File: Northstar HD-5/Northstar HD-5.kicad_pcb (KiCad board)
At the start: 2 copper layers, 190.6 x 165 mm, 123 parts, among them J1 MFM data, J2 MFM control, P1 northstar card edge, Q1 2N3904, U1A1 26LS32, U1B1 26LS31, U1C1 74S10, U1D1 74S00, U1E1 50ns_Delay, U1F1 74S04, U1H1 74LS123, U1K1 LM393, U1L1 7438, U1M1 74LS374, U2A1 100ns_Delay, U2B1 74LS161, U2C1 74LS74, U2D1 74LS175, U2E1 82S129, U2F1 74S174, U2H1 74LS283, U2J1 74LS393, U2K1 74LS393, U2L1 2114, U2M1 2114, U3A1 74S74, U3B1 74S02, U3C1 74LS161, U3D1 74LS04, U3E1 74LS161, U3F1 74LS393, U3H1 74LS273, U3J1 74LS193, U3K1 74LS164, U3L1 74LS374, U3M1 74LS166, U4A1 74S74, U4B1 74S02, U4C1 74S74, U4D1 74S04, U4F1 74LS193, U4H1 74LS193, U4J1 74LS04, U4K1 74LS244, U4L1 74LS244, U4M1 74LS244, U5D1 74S124, U5F1 74S74, U5H1 74LS32, U5J1 74LS00, U5K1 74LS279, U5L1 74LS138, U5M1 74LS138

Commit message: placed components for column 5
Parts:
- added ?: , , F.Cu at (178.6, 15.0)
- added ?: , , F.Cu at (178.6, 29.9)
- added C22: 47nF, Capacitor_THT:C_Disc_D10.0mm_W2.5mm_P5.00mm, F.Cu at (154.8, 103.2)
- added C23: 47nF, Capacitor_THT:C_Disc_D10.0mm_W2.5mm_P5.00mm, F.Cu at (154.8, 131.1)
- added C24: 47nF, Capacitor_THT:C_Disc_D10.0mm_W2.5mm_P5.00mm, F.Cu at (154.8, 145.0)
- added C25: 47nF, Capacitor_THT:C_Disc_D10.0mm_W2.5mm_P5.00mm, F.Cu at (52.6, -261.1)
- added C26: 47nF, Capacitor_THT:C_Disc_D10.0mm_W2.5mm_P5.00mm, F.Cu at (52.8, -249.9)
- added C27: 47nF, Capacitor_THT:C_Disc_D10.0mm_W2.5mm_P5.00mm, F.Cu at (53.1, -237.5)
- added C28: 47nF, Capacitor_THT:C_Disc_D10.0mm_W2.5mm_P5.00mm, F.Cu at (53.8, -91.4)
- added C29: 47nF, Capacitor_THT:C_Disc_D10.0mm_W2.5mm_P5.00mm, F.Cu at (56.1, -140.0)
- added C30: 47nF, Capacitor_THT:C_Disc_D10.0mm_W2.5mm_P5.00mm, F.Cu at (53.3, -125.2)
- added C31: 47nF, Capacitor_THT:C_Disc_D10.0mm_W2.5mm_P5.00mm, F.Cu at (53.1, -109.9)
- CR1, CR2, CR3: footprint Diode_THT:D_A-405_P12.70mm_Horizontal -> Evan's misc parts:D_A-405_P12.70mm_Horizontal_NORTH
- R1, R12, R14, R18, R19, R2, R20, R21, R22, R23, R26, R27, R28, R3, R4, R5, R6, R7: footprint Resistor_THT:R_Axial_DIN0309_L9.0mm_D3.2mm_P12.70mm_Horizontal -> Evan's misc parts:R_Axial_DIN0309_L9.0mm_D3.2mm_P12.70mm_Horizontal_NORTH
- R10, R11, R15, R16, R17, R24, R25, R29, R8, R9: footprint Resistor_THT:R_Axial_DIN0207_L6.3mm_D2.5mm_P15.24mm_Horizontal -> Evan's misc parts:R_Axial_DIN0207_L6.3mm_D2.5mm_P15.24mm_Horizontal_NORTH
- moved U5K1 397.6 mm to (160.1, 124.6), turned to 90 degrees
- moved C19 374.3 mm to (174.1, 42.2), turned to -90 degrees
- moved C3 373.9 mm to (-336.7, -137.6)
- moved R5 373.9 mm to (-337.2, -143.2)
- moved U1E1 373.9 mm to (-348.0, -143.5)
- moved TP6 371.0 mm to (53.1, -240.8)
- moved TP13 366.1 mm to (69.6, -252.0)
- moved C17 365.4 mm to (53.1, -224.8), turned to -90 degrees
- moved R13 362.2 mm to (168.4, 34.5), turned to 180 degrees
- moved R15 362.0 mm to (147.4, 36.4)
- moved R20 360.7 mm to (75.9, -183.4), turned to 180 degrees
- moved R4 351.4 mm to (154.8, 114.0), turned to -90 degrees
- moved R10 350.3 mm to (77.5, -201.4), turned to 180 degrees
- moved TP5 348.3 mm to (182.2, 12.8)
- moved U4F1 346.1 mm to (59.9, -161.8), turned to 90 degrees
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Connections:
- C19 pad 1: Net-(R13-Pad1) -> Net-(C19-Pad1)
- R13 pad 1: Net-(R13-Pad1) -> GND
- R13 pad 3: GND -> Net-(C19-Pad1)
- R14 pad 1: Net-(R13-Pad1) -> Net-(C19-Pad1)
- R15 pad 2: Net-(R13-Pad1) -> Net-(C19-Pad1)
- R2 pad 2: /Power and pullups/PU2 -> PU2
- R29 pad 1: Net-(R13-Pad1) -> Net-(C19-Pad1)
- R4 pad 2: /Power and pullups/PU4 -> PU4
- U2B1 pad 10: /HD5 Sheet 2/PU2 -> PU2
- U2B1 pad 7: /HD5 Sheet 2/PU2 -> PU2
- U2B1 pad 9: /HD5 Sheet 2/PU2 -> PU2
- U3A1 pad 13: /HD5 Sheet 2/PU2 -> PU2
- U3A1 pad 4: /HD5 Sheet 2/PU2 -> PU2
- U4A1 pad 1: /HD5 Sheet 2/PU2 -> PU2
- U4A1 pad 10: /HD5 Sheet 2/PU2 -> PU2
- U4A1 pad 13: /HD5 Sheet 2/PU2 -> PU2
- U4C1 pad 1: /HD5 Sheet 2/PU2 -> PU2
- U4C1 pad 10: /HD5 Sheet 2/PU2 -> PU2
- U5D1 pad 3: Net-(R13-Pad1) -> Net-(C19-Pad1)
- U5L1 pad 6: /HD5 Sheet 1/PU4 -> PU4
- U5M1 pad 6: /HD5 Sheet 1/PU4 -> PU4
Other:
- board text added: "+V5"
- board text added: "1"
- board text added: "2"
- board text added: "30"
- board text added: "LS00"
- board text added: "LS138"
- board text added: "LS279"
- board text added: "LS32"
- board text added: "S124"
- board text added: "S74"

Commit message: placed components and repaired multi sheet labels
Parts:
- removed ? (x2): , 
- removed the C18 at (-408.1, -52.6)
- removed the C20 at (-346.5, 102.0)
- added C32: 47nF, Evan's misc parts:C_Disc_D10.0mm_W2.5mm_P5.00mm_NORTH, F.Cu at (85.2, 5.12)
- added C33: 47nF, Evan's misc parts:C_Disc_D10.0mm_W2.5mm_P5.00mm_NORTH, F.Cu at (88.9, 19.1)
- added C34: 47nF, Evan's misc parts:C_Disc_D10.0mm_W2.5mm_P5.00mm_NORTH, F.Cu at (88.9, 47.1)
- added C35: 47nF, Evan's misc parts:C_Disc_D10.0mm_W2.5mm_P5.00mm_NORTH, F.Cu at (88.9, 75.2)
- added C36: 47nF, Evan's misc parts:C_Disc_D10.0mm_W2.5mm_P5.00mm_NORTH, F.Cu at (88.9, 103.1)
- added C37: 47nF, Evan's misc parts:C_Disc_D10.0mm_W2.5mm_P5.00mm_NORTH, F.Cu at (85.2, 131.1)
- added C38: 47nF, Evan's misc parts:C_Disc_D10.0mm_W2.5mm_P5.00mm_NORTH, F.Cu at (54.8, 5.12)
- added C39: 47nF, Evan's misc parts:C_Disc_D10.0mm_W2.5mm_P5.00mm_NORTH, F.Cu at (54.8, 19.1)
- added C40: 47nF, Evan's misc parts:C_Disc_D10.0mm_W2.5mm_P5.00mm_NORTH, F.Cu at (54.8, 47.1)
- added C41: 47nF, Evan's misc parts:C_Disc_D10.0mm_W2.5mm_P5.00mm_NORTH, F.Cu at (54.9, 66.3)
- added C42: 47nF, Evan's misc parts:C_Disc_D10.0mm_W2.5mm_P5.00mm_NORTH, F.Cu at (54.8, 75.2)
- added C43: 47nF, Evan's misc parts:C_Disc_D10.0mm_W2.5mm_P5.00mm_NORTH, F.Cu at (57.1, 103.1)
- added C44: 47nF, Evan's misc parts:C_Disc_D10.0mm_W2.5mm_P5.00mm_NORTH, F.Cu at (54.5, 131.1)
- added C45: 47nF, Evan's misc parts:C_Disc_D10.0mm_W2.5mm_P5.00mm_NORTH, F.Cu at (54.5, 145.0)
- added C46: 47nF, Evan's misc parts:C_Disc_D10.0mm_W2.5mm_P5.00mm_NORTH, F.Cu at (23.0, 5.12)
- added C47: 47nF, Evan's misc parts:C_Disc_D10.0mm_W2.5mm_P5.00mm_NORTH, F.Cu at (23.0, 19.1)
- added C48: 47nF, Evan's misc parts:C_Disc_D10.0mm_W2.5mm_P5.00mm_NORTH, F.Cu at (25.5, 33.2)
- added C49: 47nF, Evan's misc parts:C_Disc_D10.0mm_W2.5mm_P5.00mm_NORTH, F.Cu at (25.5, 47.1)
- added C50: 47nF, Evan's misc parts:C_Disc_D10.0mm_W2.5mm_P5.00mm_NORTH, F.Cu at (23.0, 61.3)
- added C51: 47nF, Evan's misc parts:C_Disc_D10.0mm_W2.5mm_P5.00mm_NORTH, F.Cu at (25.5, 75.2)
- added C52: 47nF, Evan's misc parts:C_Disc_D10.0mm_W2.5mm_P5.00mm_NORTH, F.Cu at (23.0, 101.8)
- added C53: 47nF, Evan's misc parts:C_Disc_D10.0mm_W2.5mm_P5.00mm_NORTH, F.Cu at (25.5, 131.1)
- added C54: 47nF, Evan's misc parts:C_Disc_D10.0mm_W2.5mm_P5.00mm_NORTH, F.Cu at (20.4, 145.0)
- C12, C13, C14, C15, C19, C22, C23, C24, C25, C26, C27, C28, C29, C30, C31: footprint Capacitor_THT:C_Disc_D10.0mm_W2.5mm_P5.00mm -> Evan's misc parts:C_Disc_D10.0mm_W2.5mm_P5.00mm_NORTH
- C17: renamed from C16; footprint Capacitor_THT:C_Disc_D10.0mm_W2.5mm_P5.00mm -> Evan's misc parts:C_Disc_D10.0mm_W2.5mm_P5.00mm_NORTH
- C18: renamed from C17; footprint Capacitor_THT:C_Disc_D10.0mm_W2.5mm_P5.00mm -> Evan's misc parts:C_Disc_D10.0mm_W2.5mm_P5.00mm_NORTH
- C20: renamed from C21; footprint Capacitor_THT:C_Disc_D10.0mm_W2.5mm_P5.00mm -> Evan's misc parts:C_Disc_D10.0mm_W2.5mm_P5.00mm_NORTH
- U1K1: footprint Package_DIP:DIP-8-16_W7.62mm -> Package_DIP:DIP-8_W7.62mm
- moved U3L1 576.8 mm to (91.5, 138.6), turned to 90 degrees
- moved U3M1 557.1 mm to (94.1, 152.5), turned to 90 degrees
- moved U2M1 552.6 mm to (59.7, 152.5), turned to 90 degrees
- moved U2L1 538.3 mm to (59.7, 138.6), turned to 90 degrees
- moved U1M1 535.6 mm to (25.5, 152.5), turned to 90 degrees
- moved U3K1 522.5 mm to (94.1, 124.6), turned to 90 degrees
- moved U2F1 499.2 mm to (59.7, 82.7), turned to 90 degrees
- moved U2E1 482.3 mm to (59.7, 68.7), turned to 90 degrees
- moved R25 475.7 mm to (17.9, 97.1), turned to 180 degrees
- moved U3H1 475.0 mm to (91.5, 96.7), turned to 90 degrees
- moved U2D1 466.6 mm to (59.7, 54.7), turned to 90 degrees
- moved C12 466.2 mm to (40.9, 117.0), turned to -90 degrees
- moved R24 463.1 mm to (2.63, 100.2)
- moved U3J1 457.8 mm to (94.1, 110.7), turned to 90 degrees
- moved R26 457.7 mm to (15.3, 94.0), turned to 180 degrees
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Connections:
- net /HD5 Sheet 1/RA0 renamed RA0
- net /HD5 Sheet 1/RA1 renamed RA1
- net /HD5 Sheet 1/RA2 renamed RA2
- net /HD5 Sheet 1/RA3 renamed RA3
- net /HD5 Sheet 1/RA5 renamed RA5
- net /HD5 Sheet 1/RA6 renamed RA6
- net /HD5 Sheet 1/RA7 renamed RA7
- net /HD5 Sheet 1/RA8 renamed RA8
- net /HD5 Sheet 1/RA9 renamed RA9
- net /HD5 Sheet 1/SD01 renamed SD01
- net /HD5 Sheet 1/SD02 renamed SD02
- net /HD5 Sheet 1/SD03 renamed SD03
- net /HD5 Sheet 1/SD04 renamed SD04
- net /HD5 Sheet 1/SD05 renamed SD05
- net /HD5 Sheet 1/SD06 renamed SD06
- net /HD5 Sheet 1/SD07 renamed SD07
- net /HD5 Sheet 1/WR DATA renamed WR DATA
- net /HD5 Sheet 1//CLR ADD renamed /CLR ADD
- net /HD5 Sheet 1//RD STAT renamed /RD STAT
- net /HD5 Sheet 2/2.5Mhz renamed 2.5Mhz
- net /HD5 Sheet 2/EN SYNC renamed EN SYNC
- net /HD5 Sheet 2/INT SEC P renamed INT SEC P
- net /HD5 Sheet 2/Phase Lock renamed Phase Lock
- net /HD5 Sheet 2/READ DATA renamed READ DATA
- net /HD5 Sheet 2/VCO Out renamed VCO Out
- net /HD5 Sheet 2//INT SEC P renamed /INT SEC P
- net /HD5 Sheet 2//RD CLK renamed /RD CLK
- net /Power and pullups/IO 8MHz renamed IO 8MHz
- net /Power and pullups/IO A3 renamed IO A3
- net /Power and pullups//BIO RES renamed /BIO RES
- net /Power and pullups//IO INT renamed /IO INT
- C20 pad 1: +5V -> +5VP
- J1 pad 1: /Power and pullups//SE_EC -> /SE_EC
- J1 pad 13: /Power and pullups/MFM W+ -> MFM W+
- J1 pad 14: /Power and pullups/MFM W- -> MFM W-
- J1 pad 17: /Power and pullups/MFM RD+ -> MFM RD+
- J1 pad 18: /Power and pullups/MFM RD- -> MFM RD-
- J2 pad 10: /Power and pullups//TRK0_PHI -> /TRK0_PHI
- J2 pad 12: /Power and pullups//WR FLT -> /WR FLT
- J2 pad 14: /Power and pullups/HS0 -> HS0
- J2 pad 18: /Power and pullups/HS1 -> HS1
- J2 pad 2: /Power and pullups//LOW CUR -> /LOW CUR
- J2 pad 20: /Power and pullups//INDEX -> /INDEX
- J2 pad 22: /Power and pullups//RDY -> /RDY
- J2 pad 24: /Power and pullups//STEP -> /STEP
- J2 pad 34: /Power and pullups//DIR / PRCMP -> /DIR / PRCMP
- J2 pad 4: /Power and pullups//HS2 -> /HS2
- J2 pad 6: /Power and pullups//WR GATE -> /WR GATE
- J2 pad 8: /Power and pullups//SK COMP -> /SK COMP
- P1 pad 11: /Power and pullups/IO A1 -> IO A1
- P1 pad 13: /Power and pullups//BRD -> /BRD
- P1 pad 14: /Power and pullups/IO A0 -> IO A0
- P1 pad 16: /Power and pullups//BWR -> /BWR
- P1 pad 17: /Power and pullups/IO3 -> IO3
- P1 pad 19: /Power and pullups/IO2 -> IO2
- P1 pad 20: /Power and pullups/IO4 -> IO4
- P1 pad 22: /Power and pullups/IO5 -> IO5
- P1 pad 23: /Power and pullups/IO6 -> IO6
- P1 pad 24: /Power and pullups/IO1 -> IO1
- P1 pad 25: /Power and pullups/IO0 -> IO0
- P1 pad 28: /Power and pullups/IO7 -> IO7
- P1 pad 29: /Power and pullups//SELECT -> /SELECT
- P1 pad 3: /Power and pullups//ID REQ -> IO6
- P1 pad 9: /Power and pullups/IO A2 -> IO A2
- Q1 pad 3: /HD5 Sheet 1//WR GATE -> /WR GATE
- R1 pad 2: /Power and pullups/PU1 -> PU1
- R26 pad 2: /HD5 Sheet 1/1WR GATE -> 1WR GATE
- R27 pad 2: /HD5 Sheet 1/1WR GATE -> 1WR GATE
- R3 pad 2: /Power and pullups/PU3 -> PU3
- R7 pad 1: /HD5 Sheet 2/MFM RD- -> MFM RD-
- R7 pad 2: /HD5 Sheet 2/MFM RD+ -> MFM RD+
- RN1 pad 2: /Power and pullups//INDEX -> /INDEX
- RN1 pad 3: /Power and pullups//RDY -> /RDY
- RN1 pad 4: /Power and pullups//SE_EC -> /SE_EC
- RN1 pad 5: /Power and pullups//SK0COMP -> /SK COMP
- RN1 pad 6: /Power and pullups//TRK0_PHI -> /TRK0_PHI
- RN1 pad 7: /Power and pullups//WR FLT -> /WR FLT
- RN2 pad 2: /Power and pullups/ID0 -> ID0
- RN2 pad 3: /Power and pullups/ID4 -> ID4
- RN2 pad 4: /Power and pullups/ID5 -> ID5
- RN2 pad 5: /Power and pullups/ID1 -> ID1
- RN2 pad 6: /Power and pullups/ID2 -> ID2
- RN2 pad 7: /Power and pullups/ID6 -> ID6
- RN2 pad 8: /Power and pullups/ID7 -> ID7
- RN2 pad 9: /Power and pullups/ID3 -> ID3
- TP1 pad 1: /HD5 Sheet 2/5MHz -> 5MHz
- TP12 pad 1: /HD5 Sheet 2//RD BYT RDY -> /RD BYT RDY
- TP3 pad 1: /HD5 Sheet 2/RD CLK -> RD CLK
- U1A1 pad 1: /HD5 Sheet 2/MFM RD- -> MFM RD-
- U1A1 pad 2: /HD5 Sheet 2/MFM RD+ -> MFM RD+
- U1B1 pad 5: /HD5 Sheet 1/MFM W- -> MFM W-
- U1B1 pad 6: /HD5 Sheet 1/MFM W+ -> MFM W+
- U1C1 pad 10: /HD5 Sheet 2//RD RAM -> /RD RAM
- U1C1 pad 9: /HD5 Sheet 2//HOST WR RAM -> /HOST WR RAM
- U1D1 pad 6: /HD5 Sheet 2//LD WR BYTE -> /LD WR BYTE
- U1F1 pad 9: /HD5 Sheet 2//HOST WR RAM -> /HOST WR RAM
- U1H1 pad 1: /HD5 Sheet 2//INDEX -> /INDEX
- U1H1 pad 2: /HD5 Sheet 2/PU3 -> PU3
- U1H1 pad 3: /HD5 Sheet 2//FORMAT WR -> /FORMAT WR
- U1H1 pad 9: /HD5 Sheet 2/CNTR INDEX -> CNTR INDEX
- U1L1 pad 3: /HD5 Sheet 1//STEP -> /STEP
- U1L1 pad 8: /HD5 Sheet 1//HS2 -> /HS2
- U1M1 pad 11: /HD5 Sheet 1//LD CONT -> /LD CONT
- U1M1 pad 12: /HD5 Sheet 1//LOW CUR -> /LOW CUR
- U1M1 pad 13: /HD5 Sheet 1/ID3 -> ID3
- U1M1 pad 14: /HD5 Sheet 1/ID2 -> ID2
- U1M1 pad 16: /HD5 Sheet 1/HS1 -> HS1
- U1M1 pad 17: /HD5 Sheet 1/ID1 -> ID1
- U1M1 pad 18: /HD5 Sheet 1/ID0 -> ID0
- U1M1 pad 19: /HD5 Sheet 1/HS0 -> HS0
- U1M1 pad 3: /HD5 Sheet 1/ID4 -> ID4
- U1M1 pad 4: /HD5 Sheet 1/ID5 -> ID5
- U1M1 pad 5: /HD5 Sheet 1//DIR / PRCMP -> /DIR / PRCMP
- U1M1 pad 7: /HD5 Sheet 1/ID6 -> ID6
- U1M1 pad 8: /HD5 Sheet 1/ID7 -> ID7
- U1M1 pad 9: /HD5 Sheet 1/HEADER READ -> HEADER READ
- U2B1 pad 12: /HD5 Sheet 2/RAW INDEX -> RAW INDEX
- U2C1 pad 1: /HD5 Sheet 2/RD GATE -> RD GATE
- U2C1 pad 10: /HD5 Sheet 2/PU1 -> PU1
- U2C1 pad 11: /HD5 Sheet 2/5MHz -> 5MHz
- U2C1 pad 13: /HD5 Sheet 2/PU1 -> PU1
- U2C1 pad 2: /HD5 Sheet 2/RD GATE -> RD GATE
- U2C1 pad 3: /HD5 Sheet 2/SD00 -> SD00
- U2C1 pad 4: /HD5 Sheet 2/PU1 -> PU1
- U2D1 pad 1: /HD5 Sheet 1/PU 3 -> PU3
- U2D1 pad 2: /HD5 Sheet 1/5MHz -> 5MHz
- U2E1 pad 1: /HD5 Sheet 1//DIR / PRCMP -> /DIR / PRCMP
- U2E1 pad 2: /HD5 Sheet 1/1WR GATE -> 1WR GATE
- U2E1 pad 3: /HD5 Sheet 1/5MHz -> 5MHz
- U2F1 pad 1: /HD5 Sheet 1/PU 3 -> PU3
- U2F1 pad 15: /HD5 Sheet 1/SYNC INDEX -> SYNC INDEX
- U2F1 pad 3: /HD5 Sheet 1/RAW INDEX -> RAW INDEX
- U2F1 pad 9: /HD5 Sheet 1/5MHz -> 5MHz
- U2H1 pad 11: /HD5 Sheet 2/PU3 -> PU3
- U2H1 pad 2: /HD5 Sheet 2/PU3 -> PU3
- U2H1 pad 6: /HD5 Sheet 2/PU3 -> PU3
- U2J1 pad 12: /HD5 Sheet 2/SYNC INDEX -> SYNC INDEX
- U2K1 pad 3: /HD5 Sheet 1/RA4 -> RA4
- U2L1 pad 10: /HD5 Sheet 1//WR RAM -> /WR RAM
- U2L1 pad 11: /HD5 Sheet 1/ID 3 -> ID3
- U2L1 pad 12: /HD5 Sheet 1/ID 2 -> ID2
- U2L1 pad 13: /HD5 Sheet 1/ID 1 -> ID1
- U2L1 pad 14: /HD5 Sheet 1/ID 0 -> ID0
- U2L1 pad 17: /HD5 Sheet 1/RA4 -> RA4
- U2L1 pad 8: /HD5 Sheet 1//SEL RAM -> /SEL RAM
- U2M1 pad 10: /HD5 Sheet 1//WR RAM -> /WR RAM
- U2M1 pad 11: /HD5 Sheet 1/ID 7 -> ID7
- U2M1 pad 12: /HD5 Sheet 1/ID 6 -> ID6
- U2M1 pad 13: /HD5 Sheet 1/ID 5 -> ID5
- U2M1 pad 14: /HD5 Sheet 1/ID 4 -> ID4
- U2M1 pad 17: /HD5 Sheet 1/RA4 -> RA4
- U2M1 pad 8: /HD5 Sheet 1//SEL RAM -> /SEL RAM
- U3A1 pad 5: /HD5 Sheet 2/SEP RD DATA -> SEP RD DATA
- U3B1 pad 1: /HD5 Sheet 2//WR RAM -> /WR RAM
- U3B1 pad 13: /HD5 Sheet 2//SEL RAM -> /SEL RAM
- U3B1 pad 4: /HD5 Sheet 2/RD CLK -> RD CLK
- U3B1 pad 9: /HD5 Sheet 2/RD CLK -> RD CLK
- U3C1 pad 10: /HD5 Sheet 2/PU1 -> PU1
- U3C1 pad 3: /HD5 Sheet 2/PU1 -> PU1
- U3C1 pad 7: /HD5 Sheet 2/PU1 -> PU1
- U3C1 pad 9: /HD5 Sheet 2//RD BYT RDY -> /RD BYT RDY
- U3D1 pad 10: /HD5 Sheet 2//RD DATA TO RAM -> /RD DATA TO RAM
- U3D1 pad 8: /HD5 Sheet 2//RD BYT RDY -> /RD BYT RDY
- U3E1 pad 1: /HD5 Sheet 2/1WR GATE -> 1WR GATE
- U3E1 pad 10: /HD5 Sheet 2/PU1 -> PU1
- U3E1 pad 2: /HD5 Sheet 2/5MHz -> 5MHz
- U3E1 pad 3: /HD5 Sheet 2/PU1 -> PU1
- U3E1 pad 4: /HD5 Sheet 2/PU1 -> PU1
- U3E1 pad 7: /HD5 Sheet 2/PU1 -> PU1
- U3E1 pad 9: /HD5 Sheet 2//LD WR BYTE -> /LD WR BYTE
- U3F1 pad 12: /HD5 Sheet 2/SYNC INDEX -> SYNC INDEX
- U3F1 pad 2: /HD5 Sheet 2/SYNC INDEX -> SYNC INDEX
- U3H1 pad 1: /HD5 Sheet 2/PU3 -> PU3
- U3H1 pad 11: /HD5 Sheet 2/SYNC INDEX -> SYNC INDEX
- U3J1 pad 5: /HD5 Sheet 2/PU3 -> PU3
- U3K1 pad 1: /HD5 Sheet 1/SEP RD DATA -> SEP RD DATA
- U3K1 pad 2: /HD5 Sheet 1/SEP RD DATA -> SEP RD DATA
- U3K1 pad 3: /HD5 Sheet 1/SD00 -> SD00
- U3K1 pad 8: /HD5 Sheet 1/RD CLK -> RD CLK
- U3K1 pad 9: /HD5 Sheet 1/RD GATE -> RD GATE
- U3L1 pad 1: /HD5 Sheet 1//RD DATA TO RAM -> /RD DATA TO RAM
- U3L1 pad 11: /HD5 Sheet 1//RD BYT RDY -> /RD BYT RDY
- U3L1 pad 12: /HD5 Sheet 1/ID3 -> ID3
- U3L1 pad 15: /HD5 Sheet 1/ID2 -> ID2
- U3L1 pad 16: /HD5 Sheet 1/ID1 -> ID1
- U3L1 pad 18: /HD5 Sheet 1/SD00 -> SD00
- U3L1 pad 19: /HD5 Sheet 1/ID0 -> ID0
- U3L1 pad 2: /HD5 Sheet 1/ID7 -> ID7
- U3L1 pad 5: /HD5 Sheet 1/ID6 -> ID6
- U3L1 pad 6: /HD5 Sheet 1/ID5 -> ID5
- U3L1 pad 9: /HD5 Sheet 1/ID4 -> ID4
- U3M1 pad 10: /HD5 Sheet 1/ID4 -> ID4
- U3M1 pad 11: /HD5 Sheet 1/ID5 -> ID5
- U3M1 pad 12: /HD5 Sheet 1/ID6 -> ID6
- U3M1 pad 14: /HD5 Sheet 1/ID7 -> ID7
- U3M1 pad 15: /HD5 Sheet 1//LD WR BYTE -> /LD WR BYTE
- U3M1 pad 2: /HD5 Sheet 1/ID0 -> ID0
- U3M1 pad 3: /HD5 Sheet 1/ID1 -> ID1
- U3M1 pad 4: /HD5 Sheet 1/ID2 -> ID2
- U3M1 pad 5: /HD5 Sheet 1/ID3 -> ID3
- U3M1 pad 7: /HD5 Sheet 1/5MHz -> 5MHz
- U3M1 pad 9: /HD5 Sheet 1/1WR GATE -> 1WR GATE
- U4F1 pad 5: /HD5 Sheet 2/PU4 -> PU4
- U4F1 pad 9: /HD5 Sheet 2/PU4 -> PU4
- U4H1 pad 5: /HD5 Sheet 2/PU4 -> PU4
- U4J1 pad 11: /HD5 Sheet 1//SEL RAM -> /SEL RAM
- U4J1 pad 2: /HD5 Sheet 2//H TO ID -> /H TO ID
- U4J1 pad 5: /HD5 Sheet 2/SYNC INDEX -> SYNC INDEX
- U4K1 pad 11: /HD5 Sheet 1//RDY -> /RDY
- U4K1 pad 12: /HD5 Sheet 1/HD3 -> IO3
- U4K1 pad 13: /HD5 Sheet 1/CNTR INDEX -> CNTR INDEX
- U4K1 pad 14: /HD5 Sheet 1/HD2 -> IO2
- U4K1 pad 15: /HD5 Sheet 1/R/W ACTIVE -> R/W ACTIVE
- U4K1 pad 16: /HD5 Sheet 1/HD1 -> IO1
- U4K1 pad 17: /HD5 Sheet 1/CNTR SECTOR -> CNTR SECTOR
- U4K1 pad 18: /HD5 Sheet 1/HD0 -> IO0
- U4K1 pad 2: /HD5 Sheet 1//WR FLT -> /WR FLT
- U4K1 pad 3: /HD5 Sheet 1/HD7 -> IO7
- U4K1 pad 4: /HD5 Sheet 1//SK COMP -> /SK COMP
- U4K1 pad 5: /HD5 Sheet 1/HD6 -> IO6
- U4K1 pad 6: /HD5 Sheet 1//TRK0_PHI -> /TRK0_PHI
- U4K1 pad 7: /HD5 Sheet 1/HD5 -> IO5
- U4K1 pad 8: /HD5 Sheet 1//SE_EC -> /SE_EC
- U4K1 pad 9: /HD5 Sheet 1/HD4 -> IO4
- U4L1 pad 1: /HD5 Sheet 1//H TO ID -> /H TO ID
- U4L1 pad 11: /HD5 Sheet 1/HD3 -> IO3
- U4L1 pad 12: /HD5 Sheet 1/ID4 -> ID4
- U4L1 pad 13: /HD5 Sheet 1/HD2 -> IO2
- U4L1 pad 14: /HD5 Sheet 1/ID5 -> ID5
- U4L1 pad 15: /HD5 Sheet 1/HD1 -> IO1
- U4L1 pad 16: /HD5 Sheet 1/ID6 -> ID6
- U4L1 pad 17: /HD5 Sheet 1/HD0 -> IO0
- U4L1 pad 18: /HD5 Sheet 1/ID7 -> ID7
- U4L1 pad 19: /HD5 Sheet 1//H TO ID -> /H TO ID
- U4L1 pad 2: /HD5 Sheet 1/HD7 -> IO7
- U4L1 pad 3: /HD5 Sheet 1/ID0 -> ID0
- U4L1 pad 4: /HD5 Sheet 1/HD6 -> IO6
- U4L1 pad 5: /HD5 Sheet 1/ID1 -> ID1
- U4L1 pad 6: /HD5 Sheet 1/HD5 -> IO5
- U4L1 pad 7: /HD5 Sheet 1/ID2 -> ID2
- U4L1 pad 8: /HD5 Sheet 1/HD4 -> IO4
- U4L1 pad 9: /HD5 Sheet 1/ID3 -> ID3
- U4M1 pad 1: /HD5 Sheet 1//RD RAM -> /RD RAM
- U4M1 pad 11: /HD5 Sheet 1/ID 3 -> ID3
- U4M1 pad 12: /HD5 Sheet 1/HD3 -> IO3
- U4M1 pad 13: /HD5 Sheet 1/ID 2 -> ID2
- U4M1 pad 14: /HD5 Sheet 1/HD2 -> IO2
- U4M1 pad 15: /HD5 Sheet 1/ID 1 -> ID1
- U4M1 pad 16: /HD5 Sheet 1/HD1 -> IO1
- U4M1 pad 17: /HD5 Sheet 1/ID 0 -> ID0
- U4M1 pad 18: /HD5 Sheet 1/HD0 -> IO0
- U4M1 pad 19: /HD5 Sheet 1//RD RAM -> /RD RAM
- U4M1 pad 2: /HD5 Sheet 1/ID 7 -> ID7
- U4M1 pad 3: /HD5 Sheet 1/HD7 -> IO7
- U4M1 pad 4: /HD5 Sheet 1/ID 6 -> ID6
- U4M1 pad 5: /HD5 Sheet 1/HD6 -> IO6
- U4M1 pad 6: /HD5 Sheet 1/ID 5 -> ID5
- U4M1 pad 7: /HD5 Sheet 1/HD5 -> IO5
- U4M1 pad 8: /HD5 Sheet 1/ID 4 -> ID4
- U4M1 pad 9: /HD5 Sheet 1/HD4 -> IO4
- U5F1 pad 1: /HD5 Sheet 2/PU4 -> PU4
- U5F1 pad 10: /HD5 Sheet 2//START READ -> /START READ
- U5F1 pad 4: /HD5 Sheet 2//LD SEC CNT -> /LD SEC CNT
- U5F1 pad 9: /HD5 Sheet 2/RD GATE -> RD GATE
- U5H1 pad 11: /HD5 Sheet 2/R/W ACTIVE -> R/W ACTIVE
- U5H1 pad 13: /HD5 Sheet 2/1WR GATE -> 1WR GATE
- U5J1 pad 12: /HD5 Sheet 2/HEADER READ -> HEADER READ
- U5J1 pad 13: /HD5 Sheet 2/RA4 -> RA4
- U5J1 pad 4: /HD5 Sheet 2//HOST WR RAM -> /HOST WR RAM
- U5J1 pad 5: /HD5 Sheet 2//LD CONT -> /LD CONT
- U5K1 pad 11: /HD5 Sheet 2//FORMAT WR -> /FORMAT WR
- U5K1 pad 12: /HD5 Sheet 2//START WR -> /START WR
- U5K1 pad 14: /HD5 Sheet 2//START READ -> /START READ
- U5K1 pad 15: /HD5 Sheet 2//START SYNC -> /START SYNC
- U5K1 pad 3: /HD5 Sheet 2//FORMAT WR -> /FORMAT WR
- U5K1 pad 4: /HD5 Sheet 2/CNTR INDEX -> CNTR INDEX
- U5K1 pad 5: /HD5 Sheet 2//CLR SEC -> /CLR SEC
- U5K1 pad 7: /HD5 Sheet 2/CNTR SECTOR -> CNTR SECTOR
- U5K1 pad 9: /HD5 Sheet 2/1WR GATE -> 1WR GATE
- U5L1 pad 1: /HD5 Sheet 1/IO A0 -> IO A0
- U5L1 pad 10: /HD5 Sheet 1//START READ -> /START READ
- U5L1 pad 11: /HD5 Sheet 1//START SYNC -> /START SYNC
- U5L1 pad 12: /HD5 Sheet 1//CLR SEC -> /CLR SEC
- U5L1 pad 15: /HD5 Sheet 1//RD RAM -> /RD RAM
- U5L1 pad 2: /HD5 Sheet 1/IO A1 -> IO A1
- U5L1 pad 3: /HD5 Sheet 1/IO A2 -> IO A2
- U5L1 pad 4: /HD5 Sheet 1//BRD -> /BRD
- U5L1 pad 5: /HD5 Sheet 1//SELECT -> /SELECT
- U5L1 pad 7: /HD5 Sheet 1//FORMAT WR -> /FORMAT WR
- U5L1 pad 9: /HD5 Sheet 1//START WR -> /START WR
- U5M1 pad 1: /HD5 Sheet 1/IO A0 -> IO A0
- U5M1 pad 10: /HD5 Sheet 1//LD SEC CNT -> /LD SEC CNT
- U5M1 pad 2: /HD5 Sheet 1/IO A1 -> IO A1
- U5M1 pad 3: /HD5 Sheet 1/IO A2 -> IO A2
- U5M1 pad 4: /HD5 Sheet 1//BWR -> /BWR
- U5M1 pad 5: /HD5 Sheet 1//SELECT -> /SELECT
- U5M1 pad 7: /HD5 Sheet 1//HOST WR RAM -> /HOST WR RAM
- U5M1 pad 9: /HD5 Sheet 1//LD CONT -> /LD CONT
- XTL1 pad 1: Net-(R5-Pad2) -> Net-(C4-Pad1)
- XTL1 pad 2: Net-(C4-Pad1) -> Net-(R5-Pad2)
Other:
- board text added: "+5"
- board text added: "100 nS"
- board text added: "LS04"
- board text added: "LS161"
- board text added: "LS164"
- board text added: "LS166"
- board text added: "LS193"
- board text added: "LS273"
- board text added: "LS283"
- board text added: "LS374"
- board text added: "LS393"
- board text added: "MHDWP"
- board text added: "S02"
- board text added: "S04"
- board text added: "S161"
- board text added: "S174"
- board text added: "S175"

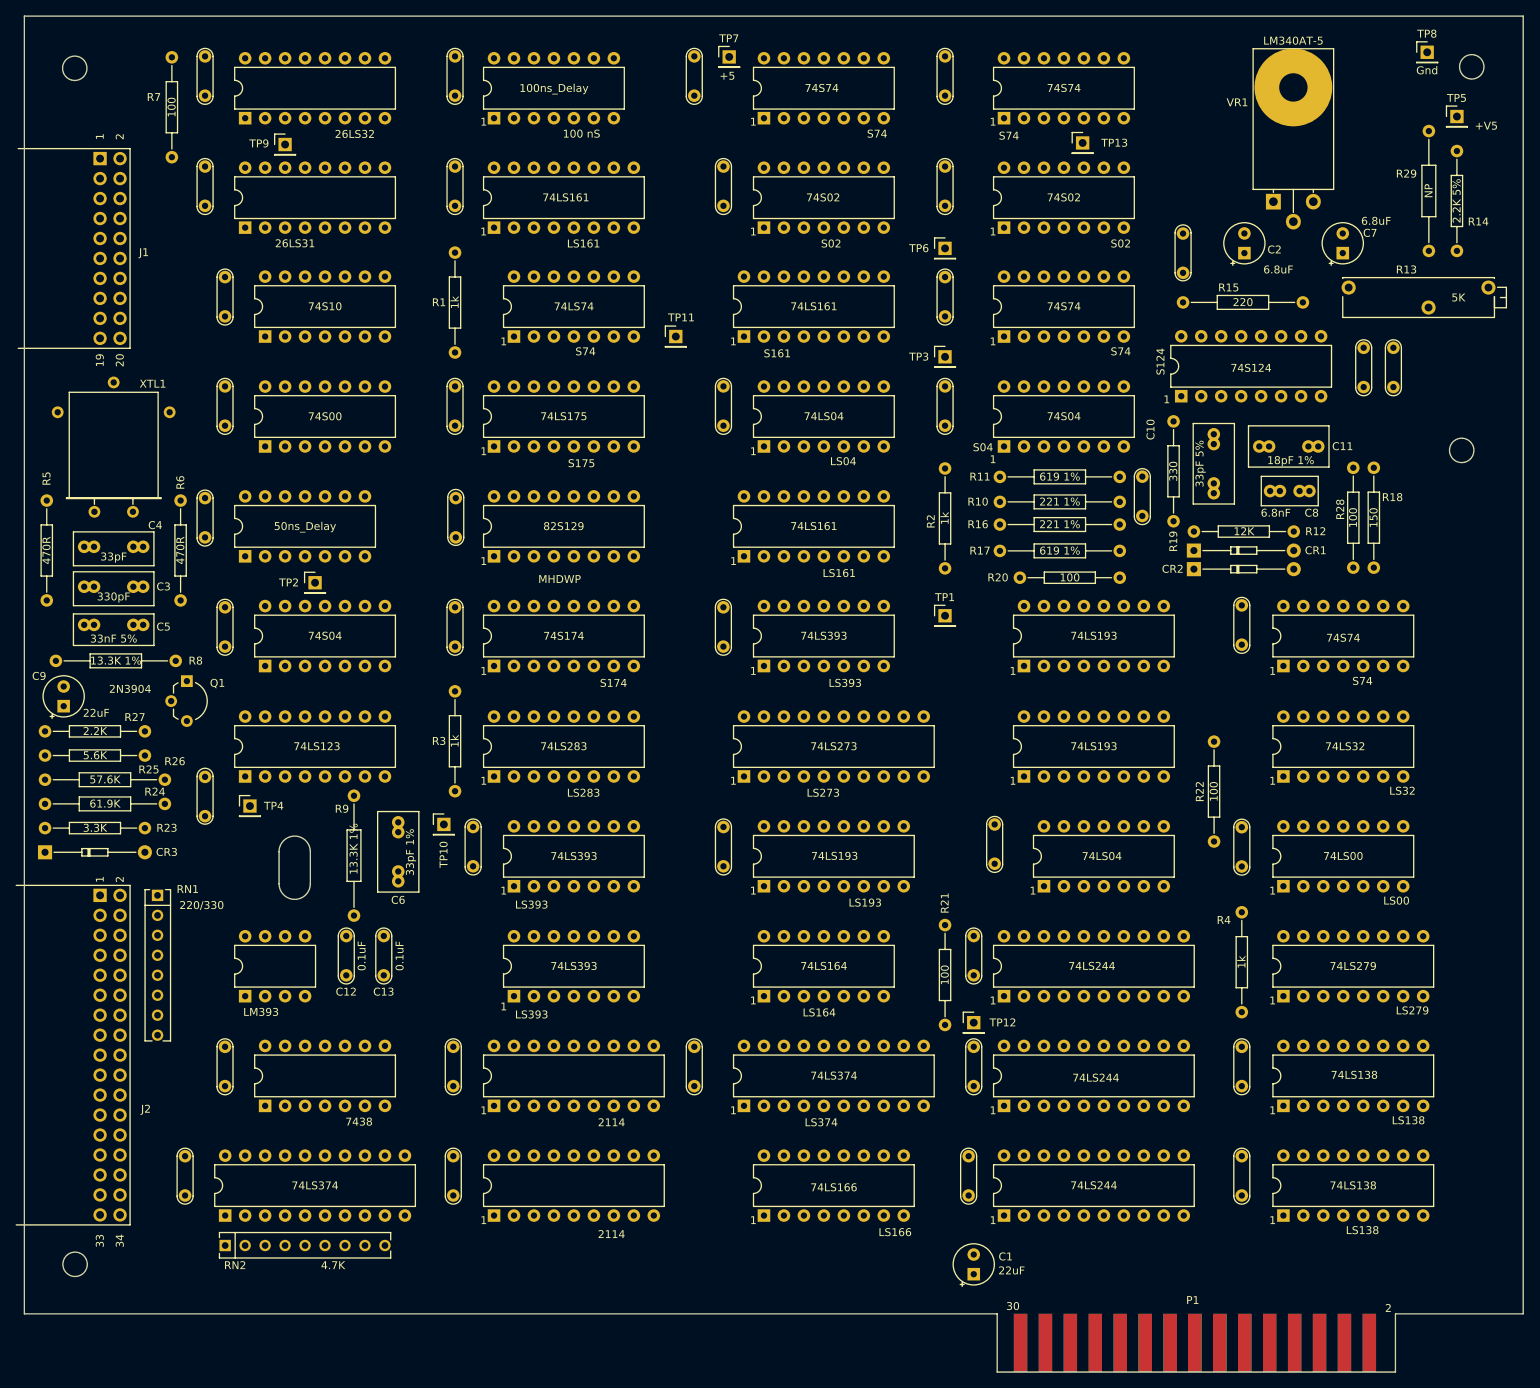
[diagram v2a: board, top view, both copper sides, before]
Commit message: finished signal routing top and bottom (assumed correct)
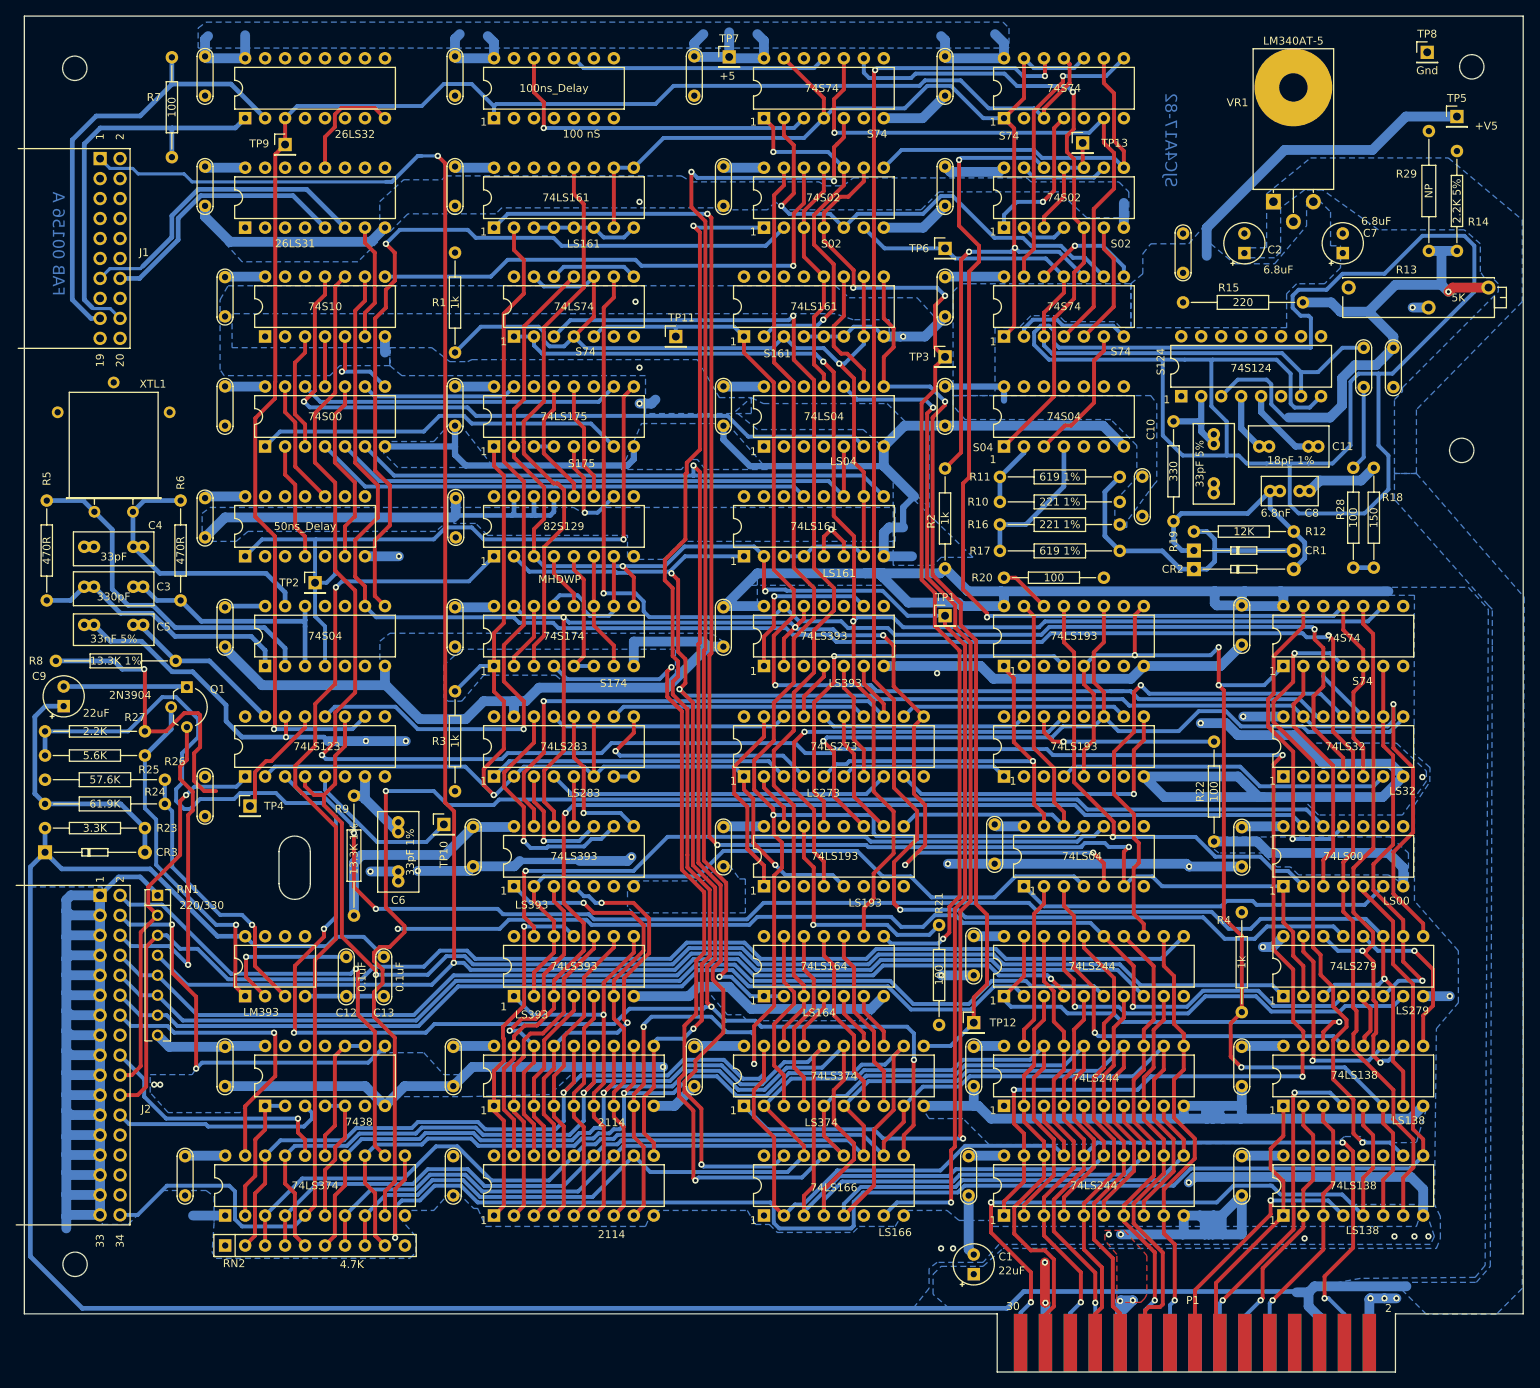
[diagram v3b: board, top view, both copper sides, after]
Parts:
- RN2: footprint Package_SIP:SIP-9_21.54x3mm_P2.54mm -> Resistor_THT:R_Array_SIP10
- moved R8 15.2 mm to (4.01, 82.0), turned to 0 degrees
- moved C12 2.65 mm to (40.9, 119.6)
- moved C13 2.65 mm to (45.7, 119.6)
- moved U4F1 2.54 mm to (124.6, 82.7)
- moved U4H1 2.54 mm to (124.6, 96.7)
- moved U4J1 2.54 mm to (127.1, 110.7)
- moved R20 2.02 mm to (137.3, 71.4)
- moved Q1 0.76 mm to (20.7, 85.3)
- moved R21 0.76 mm to (116.3, 128.3)
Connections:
- U4K1 pad 13: CNTR INDEX -> R/W ACTIVE
- U4K1 pad 15: R/W ACTIVE -> CNTR INDEX
- U4M1 pad 12: IO3 -> IO4
- U4M1 pad 14: IO2 -> IO5
- U4M1 pad 16: IO1 -> IO6
- U4M1 pad 18: IO0 -> IO7
- U4M1 pad 3: IO7 -> IO0
- U4M1 pad 5: IO6 -> IO1
- U4M1 pad 7: IO5 -> IO2
- U4M1 pad 9: IO4 -> IO3
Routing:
- net GND: track 0.00 -> 1397.9 mm, vias 0 -> 38
- net +5V: track 0.00 -> 425.3 mm, vias 0 -> 6
- net 1WR GATE: track 0.00 -> 405.5 mm, vias 0 -> 7
- net +12V: track 0.00 -> 290.8 mm
- net /RD RAM: track 0.00 -> 288.6 mm, vias 0 -> 4
- net /SE_EC: track 0.00 -> 281.7 mm, vias 0 -> 2
- net /HOST WR RAM: track 0.00 -> 250.7 mm, vias 0 -> 1
- net /SEL RAM: track 0.00 -> 209.9 mm, vias 0 -> 3
- net READ DATA: track 0.00 -> 206.2 mm, vias 0 -> 1
- net Net-(U2B1-Pad1): track 0.00 -> 203.4 mm, vias 0 -> 3
- net EN SYNC: track 0.00 -> 194.2 mm, vias 0 -> 3
- net /LD CONT: track 0.00 -> 194.1 mm, vias 0 -> 1
- net 5MHz: track 0.00 -> 192.3 mm, vias 0 -> 3
- net RD GATE: track 0.00 -> 189.0 mm, vias 0 -> 2
- net /FORMAT WR: track 0.00 -> 186.7 mm, vias 0 -> 3
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- added copper zone on B.Cu, net +12V
- added copper zone on B.Cu, net +5V
- added copper zone on B.Cu, net +5VP
- added copper zone on B.Cu, net GND
- added copper zone on F.Cu, net GND
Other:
- board text added: "FAB 00156 A"
- board text added: "SJC4A17-82"

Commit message: finished initial layout
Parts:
- added G***: LOGO, Evan's misc parts:OSHW gear, B.Cu at (19.6, 42.2)
- added G***: LOGO, Evan's misc parts:Evan Logo, B.Cu at (146.6, 3.05)
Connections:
- XTL1 pad 3: (no net) -> GND
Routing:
- net GND: track 1397.9 -> 1858.5 mm
- net +5V: track 425.3 -> 638.3 mm, vias 6 -> 11
- net (no net): track 0.00 -> 37.2 mm
- net CNTR INDEX: track 132.7 -> 161.5 mm
- net /H TO ID: track 21.4 -> 30.0 mm
- net +5VP: track 50.5 -> 56.8 mm
- net IO A1: track 34.3 -> 35.8 mm
- net /BRD: track 42.7 -> 43.9 mm
- added copper zone on F.Cu, net +5V
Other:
- board text added: "*"
- board text added: "3"
- board text added: "4"
- board text added: "5"
- board text added: "A"
- board text added: "ADVANTAGE HD-5 CONTROLLER"
- board text added: "B"
- board text added: "C"
- board text added: "D"
- board text added: "E"
- board text added: "F"
- board text added: "H"
- board text added: "J"
- board text added: "K"
- board text added: "L"
- board text added: "LS 244"
- board text added: "LS244"
- board text added: "M"
- board text added: "MADE IN USA"
- board text added: "NorthStar"
- board text added: "S/N"
- board text added: "abzman2k.wordpress.com"
- board text added: "© NSCI 81 ASSY 00157"
